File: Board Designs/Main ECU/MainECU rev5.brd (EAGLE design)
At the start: 120.6 x 78.9 mm, 164 parts, among them Q10 MMBT3904LT3G, Q11 MMBT3904LT3G, Q9 MMBT3904LT3G, X1 CONNECTOR-37, X2 CONNECTOR-4AUTOSPORT, X3 CONNECTOR-4NANO-FIT-VERTICAL-4, X4 CONNECTOR-4NANO-FIT-VERTICAL-4

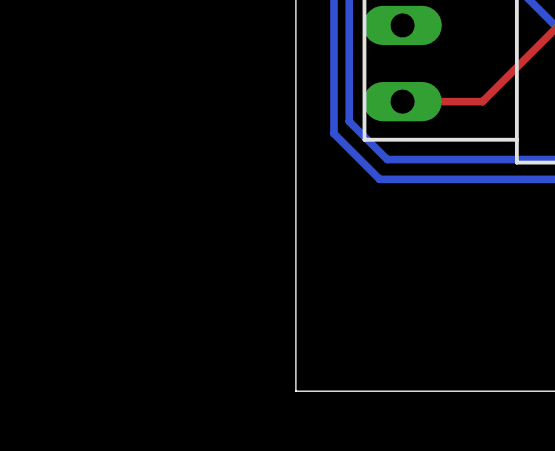
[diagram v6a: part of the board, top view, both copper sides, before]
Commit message: Began replacing BJT with mosfets
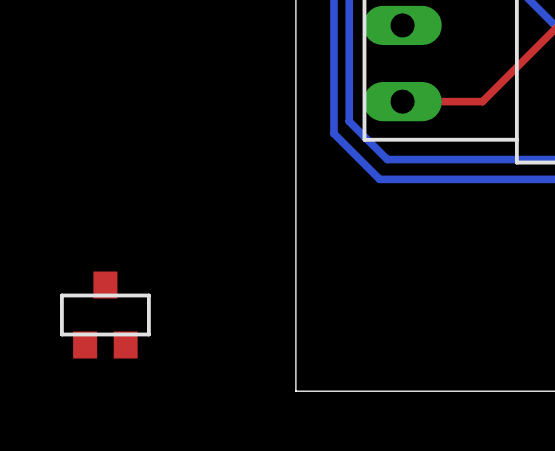
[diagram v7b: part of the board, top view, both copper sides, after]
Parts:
- added Q1: (no value), HyTechDevices:SOT23
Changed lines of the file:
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@@
 <?xml version="1.0" encoding="utf-8"?>
 <!DOCTYPE eagle SYSTEM "eagle.dtd">
-<eagle version="9.2.2">
+<eagle version="9.3.0">
 <drawing>
 <settings>
-<setting alwaysvectorfont="no"/>
+<setting alwaysvectorfont="yes"/>
 <setting verticaltext="up"/>
 </settings>
-<grid distance="5" unitdist="mil" unit="mil" style="lines" multiple="1" display="yes" altdistance="5" altunitdist="mil" altunit="mil"/>
+<grid distance="50" unitdist="mil" unit="mil" style="lines" multiple="1" display="yes" altdistance="5" altunitdist="mil" altunit="mil"/>
 <layers>
 <layer number="1" name="Top" color="4" fill="1" visible="yes" active="yes"/>
@@
 <attribute name="VALUE" x="116.586" y="62.2808" size="0.3048" layer="28" rot="MR0" align="top-center"/>
 </element>
+<element name="Q1" library="HyTechDevices" package="SOT23" value="" x="-6.35" y="2.54" smashed="yes"/>
 </elements>
 <signals>

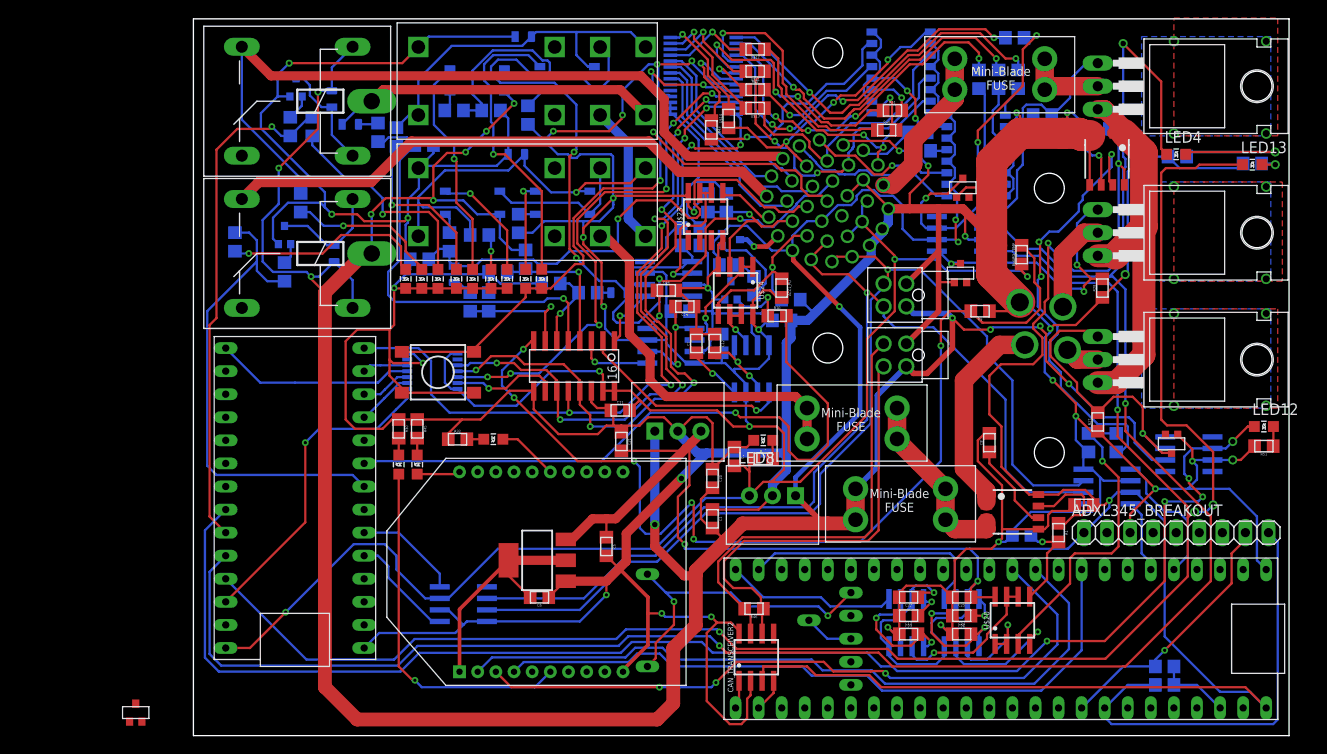
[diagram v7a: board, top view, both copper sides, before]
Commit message: Replaced BJTs with MOSFETs, but need to do layout
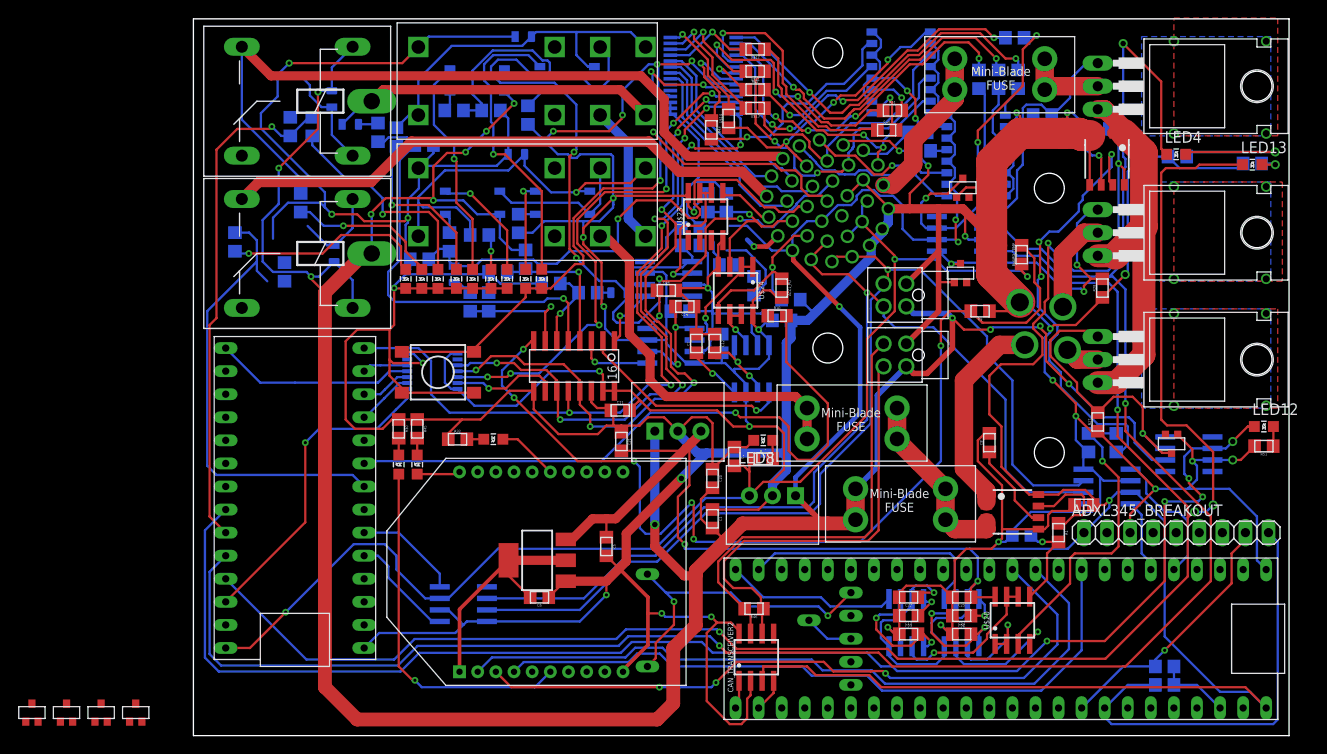
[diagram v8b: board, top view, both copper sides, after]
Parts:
- removed Q1: (no value), HyTechDevices:SOT23
- Q10, Q11, Q9: value MMBT3904LT3G -> (none)
- R10: value 2.2k -> 10k
- R47, R50: value 1k -> 10k
- R49: value 1.2k -> 10k
- U$15: value SMMBT2907ALT1G -> P-CHANNEL_MOSFET_DMP3099L-7
- moved U$15 92.9 mm to (-17.8, 2.54), flipped to the top, turned to 0 degrees
- moved Q10 86.7 mm to (-14.0, 2.54), flipped to the top
- moved Q11 72.1 mm to (-10.2, 2.54), flipped to the top
- moved Q9 55.1 mm to (-6.35, 2.54), flipped to the top
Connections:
- removed net N$17: Q10.3, R48.2, R49.1
- removed net N$26: Q11.1, R50.2
- removed net N$65: Q9.1, R47.2
- removed net N$7: Q10.1, R10.1
- net +12V: now also U$15.3; no longer U$15.2
- net BRAKE_LIGHT: now also U$15.2; no longer U$15.3
- net BRAKE_LIGHT_CTRL: now also Q10.1
- net GND: now also Q10.3, Q11.3, Q9.3, R10.1, R47.2, R49.1, R50.2; no longer Q10.2, Q11.2, Q9.2
- net INVERTER_CTRL: now also Q9.1
- net N$27: now also Q11.2; no longer Q11.3
- net N$58: now also Q10.2, R48.2
- net N$66: now also Q9.2; no longer Q9.3
- net SOFTWARE_SHUTDOWN: now also Q11.1
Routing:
- net N$7: track 6.32 -> 0.00 mm, vias 1 -> 0
- net N$17: track 4.40 -> 0.00 mm
- net GND: track 849.3 -> 845.8 mm
- net N$26: track 2.84 -> 0.00 mm
- net N$66: track 12.4 -> 9.82 mm
- net +12V: track 416.7 -> 414.2 mm
- net N$65: track 2.32 -> 0.00 mm
- net INVERTER_CTRL: track 52.6 -> 50.7 mm
- net N$58: track 9.23 -> 10.1 mm
- net BRAKE_LIGHT: track 4.96 -> 4.18 mm
- net N$27: track 12.2 -> 11.4 mm
